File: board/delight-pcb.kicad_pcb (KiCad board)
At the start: 2 copper layers, 304.9 x 114.5 mm, 197 parts, among them J1 AVR-ISP-6, SW0 KEYSW, SW1 KEYSW, SW10 KEYSW, SW11 KEYSW, SW12 KEYSW, SW13 KEYSW, SW14 KEYSW, SW15 KEYSW, SW16 KEYSW, SW17 KEYSW, SW18 KEYSW, SW19 KEYSW, SW2 KEYSW, SW20 KEYSW, SW21 KEYSW, SW22 KEYSW, SW23 KEYSW, SW24 KEYSW, SW25 KEYSW, SW26 KEYSW, SW27 KEYSW, SW28 KEYSW, SW28-2 KEYSW, SW29 KEYSW, SW3 KEYSW, SW30 KEYSW, SW31 KEYSW, SW32 KEYSW, SW33 KEYSW, SW34 KEYSW, SW35 KEYSW, SW36 KEYSW, SW37 KEYSW, SW38 KEYSW, SW39 KEYSW, SW4 KEYSW, SW40 KEYSW, SW41 KEYSW, SW42 KEYSW, SW42-2 KEYSW, SW43 KEYSW, SW44 KEYSW, SW44-2 KEYSW, SW45 KEYSW, SW46 KEYSW, SW47 KEYSW, SW48 KEYSW, SW49 KEYSW, SW5 KEYSW, SW50 KEYSW, SW51 KEYSW, SW52 KEYSW, SW53 KEYSW, SW54 KEYSW, SW55 KEYSW, SW56 KEYSW, SW57 KEYSW, SW58 KEYSW, SW59 KEYSW, SW59-2 KEYSW, SW6 KEYSW, SW60 KEYSW, SW60-2 KEYSW, SW61 KEYSW, SW62-2 KEYSW, SW63 KEYSW, SW63-2 KEYSW, SW64 KEYSW, SW64-2 KEYSW, SW65 KEYSW, SW65-2 KEYSW, SW66 KEYSW, SW67 KEYSW, SW68 KEYSW, SW69 KEYSW, SW7 KEYSW, SW8 KEYSW, SW9 KEYSW, U1 ATmega32A-PU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

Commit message: Cleanup all the tracks after the footprint switch.
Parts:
- removed the REF** at (118.6, 115.6)
- removed the REF** at (71.9, 134.9)
- removed the REF** at (217.1, 178.4)
- added REF**: MountingHole_2.2mm_M2_Pad, MountingHole:MountingHole_2.2mm_M2_Pad, F.Cu at (205.7, 175.0)
- added REF**: MountingHole_2.2mm_M2_Pad, MountingHole:MountingHole_2.2mm_M2_Pad, F.Cu at (70.6, 135.4)
- moved REF** 40.4 mm to (348.7, 105.9)
- moved REF** 24.2 mm to (188.5, 133.9)
- moved REF** 23.1 mm to (350.3, 172.7)
- moved REF** 15.8 mm to (90.2, 173.5)
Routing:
- net Net-(D17-Pad2): track 138.9 -> 129.5 mm
- net row4: track 600.2 -> 607.7 mm
- net col1: track 163.5 -> 167.6 mm
- net Net-(D30-Pad2): track 152.6 -> 155.6 mm
- net Net-(D28-Pad2): track 56.2 -> 58.8 mm
- net Net-(D13-Pad2): track 67.2 -> 69.8 mm
- net Net-(D42-Pad2): track 81.2 -> 83.7 mm
- net Net-(D57-Pad2): track 72.5 -> 75.0 mm
- net Net-(D65-Pad2): track 21.1 -> 19.9 mm
- net Net-(D15-Pad2): track 155.7 -> 154.8 mm
- net col6: track 141.2 -> 142.1 mm
- net Net-(D3-Pad2): track 147.3 -> 146.7 mm
- net GND: vias 23 -> 22

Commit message: Traces for power and pairs
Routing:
- net col4: track 100.7 -> 106.7 mm
- net Net-(D1-Pad2): track 159.8 -> 164.5 mm
- net col10: track 210.2 -> 214.4 mm
- net Net-(D12-Pad2): track 79.4 -> 82.7 mm
- net col3: track 141.7 -> 145.0 mm
- net Net-(D27-Pad2): track 56.0 -> 59.3 mm
- net Net-(D47-Pad2): track 160.6 -> 157.7 mm
- net col11: track 213.2 -> 216.1 mm
- net Net-(D41-Pad2): track 70.0 -> 67.3 mm
- net Net-(D55-Pad2): track 91.9 -> 89.4 mm
- net Net-(D15-Pad2): track 154.8 -> 157.0 mm
- net col2: track 146.7 -> 148.9 mm
- net Net-(D11-Pad2): track 76.4 -> 78.4 mm
- net col12: track 226.8 -> 228.6 mm
- net Net-(D26-Pad2): track 55.0 -> 56.7 mm
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
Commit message: Footprint schema updated
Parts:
- D59, D60, D61, D62, D63, D64, D65, D66, D67, D68, D69: footprint cftkb:D_DO-35_SOD27_P5.08mm_Horizontal -> Diode_THT:D_DO-35_SOD27_P7.62mm_Horizontal
- moved D61 5.34 mm to (112.3, 174.0)
- moved D64 0.51 mm to (271.8, 174.0)
- moved D68 0.51 mm to (343.4, 174.0)
- moved D69 0.51 mm to (362.5, 174.0)
- moved D62 0.36 mm to (126.7, 174.0)
- moved D65 0.25 mm to (286.5, 174.0)
- moved D66 0.25 mm to (305.3, 174.0)
- moved D67 0.25 mm to (324.6, 174.0)
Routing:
- net Net-(D61-Pad2): track 16.9 -> 10.4 mm
- net row4: track 607.7 -> 602.3 mm
- net Net-(D64-Pad2): track 10.3 -> 11.3 mm
- net col14: track 267.3 -> 268.3 mm
- net col13: track 266.0 -> 267.0 mm
- net Net-(D62-Pad2): track 22.3 -> 23.1 mm
- net Net-(D66-Pad2): track 5.67 -> 6.19 mm
- net Net-(D63-Pad2): track 15.5 -> 15.0 mm
- net Net-(D60-Pad2): track 9.92 -> 9.39 mm
- net Net-(D69-Pad2): track 5.41 -> 5.93 mm
- net Net-(D68-Pad2): track 5.41 -> 5.93 mm

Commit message: Once more with layouts
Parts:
- moved D62 0.36 mm to (126.5, 173.7)
- moved D63 0.36 mm to (197.1, 173.7)
- moved D64 0.36 mm to (271.5, 173.7)
- moved D60 0.25 mm to (85.6, 173.7)
- moved D61 0.25 mm to (112.3, 173.7)
- moved D65 0.25 mm to (286.5, 173.7)
- moved D66 0.25 mm to (305.3, 173.7)
- moved D67 0.25 mm to (324.6, 173.7)
- moved D68 0.25 mm to (343.4, 173.7)
- moved D69 0.25 mm to (362.5, 173.7)
- moved D59 0.25 mm to (85.6, 154.7)
- moved SW63 0.17 mm to (195.9, 182.4)
- moved SW61 0.15 mm to (100.3, 182.4)
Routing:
- net row4: track 602.3 -> 601.2 mm
- net Net-(D69-Pad2): track 5.93 -> 6.69 mm
- net Net-(D68-Pad2): track 5.93 -> 6.69 mm
- net Net-(D67-Pad2): track 6.08 -> 6.59 mm
- net Net-(D66-Pad2): track 6.19 -> 6.70 mm
- net Net-(D65-Pad2): track 20.3 -> 20.8 mm

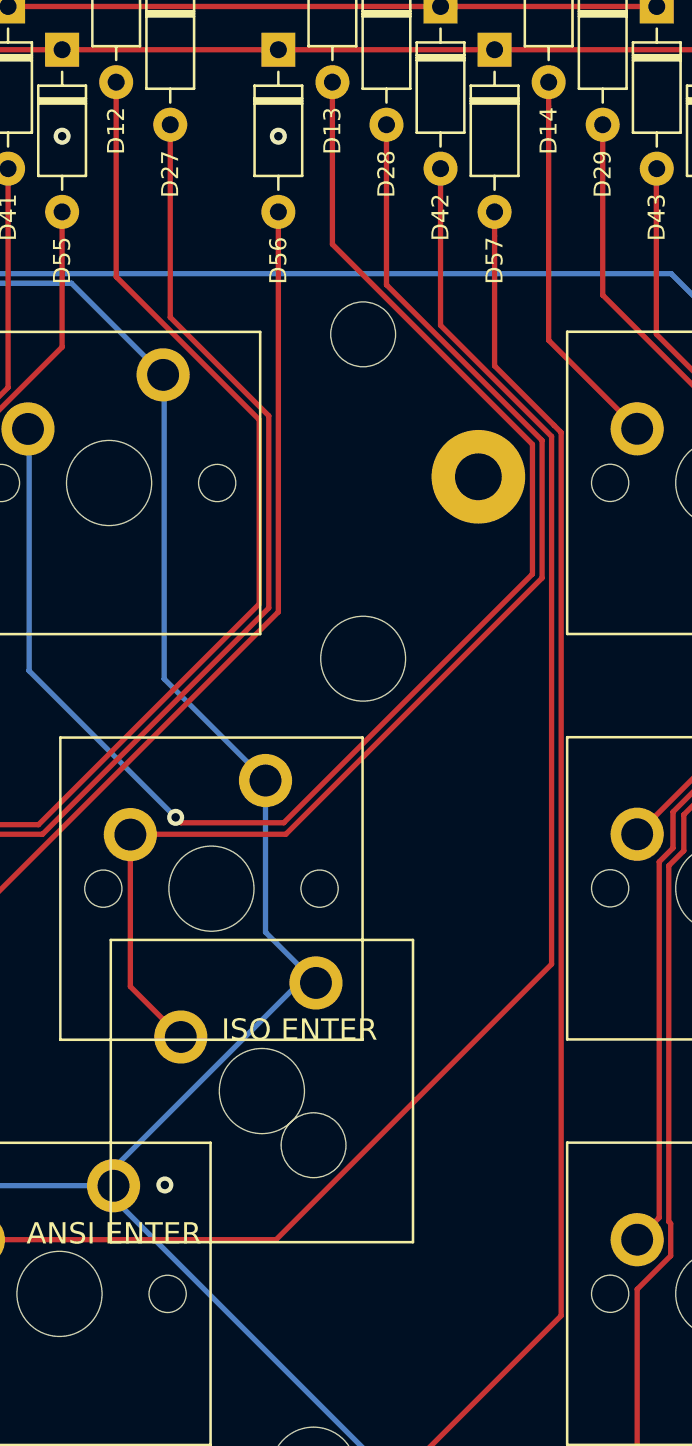
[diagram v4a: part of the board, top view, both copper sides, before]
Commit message: mounting holes movement.
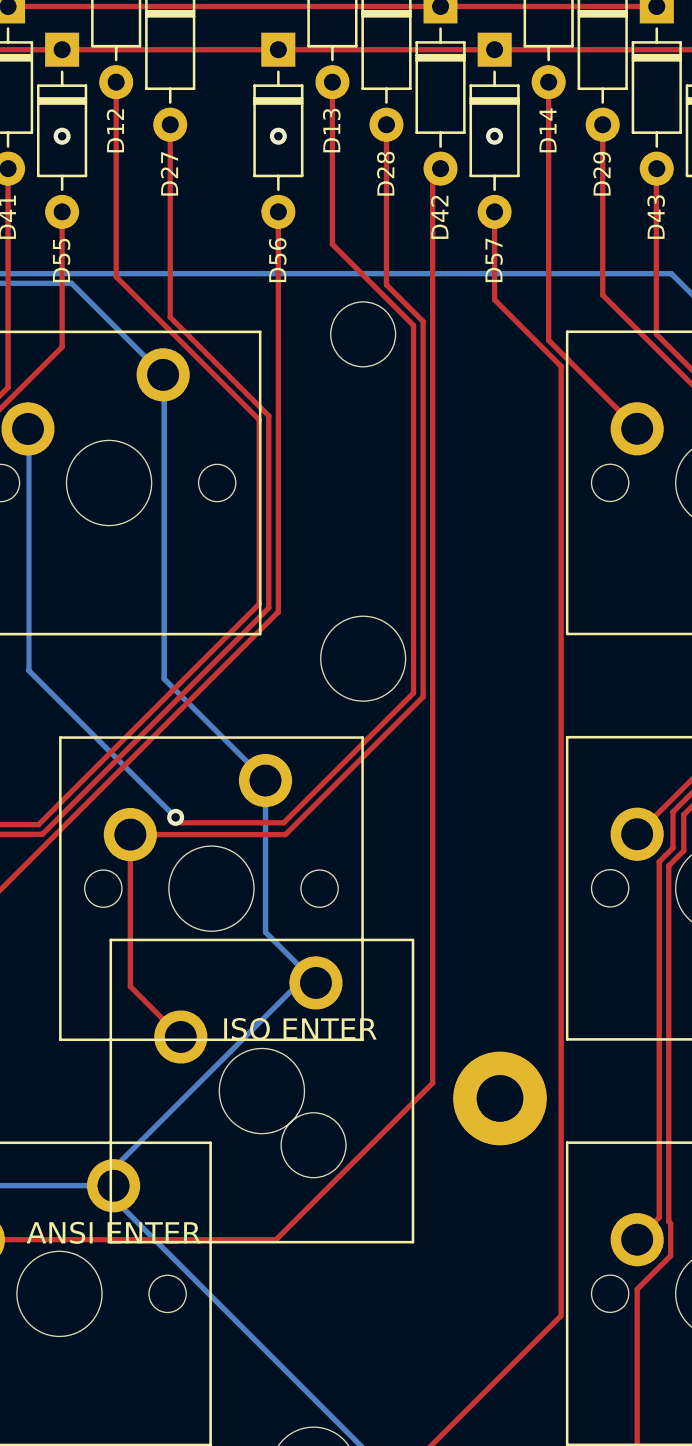
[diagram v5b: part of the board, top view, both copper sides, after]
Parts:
- moved REF** 29.2 mm to (349.8, 135.1)
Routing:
- net Net-(D13-Pad2): track 69.8 -> 65.2 mm
- net Net-(D28-Pad2): track 59.2 -> 54.5 mm
- net Net-(D42-Pad2): track 83.7 -> 79.4 mm
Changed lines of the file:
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@@
     (thickness 1.6)
     (drawings 36)
-    (tracks 1179)
+    (tracks 1175)
     (zones 0)
     (modules 196)
@@
   )
   (module MountingHole:MountingHole_2.2mm_M2_Pad (layer F.Cu)
-    (at 348.742 105.918)
+    (at 349.758 135.128)
     (descr "Mounting Hole 2.2mm, M2")
     (tags "mounting hole 2.2mm m2")
@@
   (via (at 339.344 89.916) (size 0.8) (drill 0.4) (layers F.Cu B.Cu) (net 1))
   (via (at 298.196 120.142) (size 0.8) (drill 0.4) (layers F.Cu B.Cu) (net 1))
-  (via (at 334.01 139.192) (size 0.8) (drill 0.4) (layers F.Cu B.Cu) (net 1))
-  (via (at 317.5 120.142) (size 0.8) (drill 0.4) (layers F.Cu B.Cu) (net 1))
   (via (at 290.322 178.562) (size 0.8) (drill 0.4) (layers F.Cu B.Cu) (net 1))
   (via (at 322.58 140.462) (size 0.8) (drill 0.4) (layers F.Cu B.Cu) (net 1))
+  (via (at 349.504 89.916) (size 0.8) (drill 0.4) (layers F.Cu B.Cu) (net 1))
+  (via (at 317.5 120.142) (size 0.8) (drill 0.4) (layers F.Cu B.Cu) (net 1))
   (segment (start 122.008 81.495) (end 122.008 82.245) (width 0.381) (layer F.Cu) (net 2))
   (segment (start 117.758 82.245) (end 117.758 81.495) (width 0.381) (layer F.Cu) (net 2))
@@
   (segment (start 310.388 121.92) (end 310.73174 122.26374) (width 0.25) (layer F.Cu) (net 15))
   (segment (start 327.62825 103.66375) (end 327.62825 115.03025) (width 0.25) (layer B.Cu) (net 16))
-  (segment (start 334.518 121.92) (end 334.772 122.174) (width 0.25) (layer F.Cu) (net 16) (status 40000))
-  (segment (start 334.772 122.174) (end 339.598 122.174) (width 0.25) (layer F.Cu) (net 16) (status 40000))
-  (segment (start 339.598 122.174) (end 351.282 110.49) (width 0.25) (layer F.Cu) (net 16) (status 40000))
-  (segment (start 351.282 110.49) (end 351.282 104.394) (width 0.25) (layer F.Cu) (net 16) (status 40000))
-  (segment (start 351.282 104.394) (end 341.884 94.996) (width 0.25) (layer F.Cu) (net 16) (status 40000))
-  (segment (start 341.884 94.996) (end 341.884 87.376) (width 0.25) (layer F.Cu) (net 16) (status 40000))
   (via (at 334.518 121.92) (size 0.8) (drill 0.4) (layers F.Cu B.Cu) (net 16))
   (segment (start 327.62825 115.03025) (end 334.518 121.92) (width 0.25) (layer B.Cu) (net 16))
+  (segment (start 345.694 98.806) (end 341.884 94.996) (width 0.25) (layer F.Cu) (net 16))
+  (segment (start 345.694 116.078) (end 345.694 98.806) (width 0.25) (layer F.Cu) (net 16) (status 40000))
+  (segment (start 341.884 94.996) (end 341.884 87.376) (width 0.25) (layer F.Cu) (net 16))
+  (segment (start 339.598 122.174) (end 345.694 116.078) (width 0.25) (layer F.Cu) (net 16))
+  (segment (start 334.772 122.174) (end 339.598 122.174) (width 0.25) (layer F.Cu) (net 16))
+  (segment (start 334.518 121.92) (end 334.772 122.174) (width 0.25) (layer F.Cu) (net 16))
   (segment (start 352.044 88.50737) (end 352.044 87.376) (width 0.25) (layer F.Cu) (net 17))
-  (segment (start 352.044 99.5045) (end 352.044 88.50737) (width 0.25) (layer F.Cu) (net 17))
-  (segment (start 356.20325 103.66375) (end 352.044 99.5045) (width 0.25) (layer F.Cu) (net 17))
+  (segment (start 352.044 99.5045) (end 352.044 88.50737) (width 0.25) (layer F.Cu) (net 17) (status 40000))
+  (segment (start 356.20325 103.66375) (end 352.044 99.5045) (width 0.25) (layer F.Cu) (net 17) (status 40000))
   (segment (start 212.344 97.27918) (end 212.344 89.376) (width 0.25) (layer F.Cu) (net 18) (status 40000))
   (segment (start 211.405208 98.217972) (end 212.344 97.27918) (width 0.25) (layer F.Cu) (net 18) (status 40000))
@@
   (segment (start 338.89399 112.0816) (end 338.893989 103.053579) (width 0.25) (layer F.Cu) (net 31))
   (segment (start 338.893989 103.053579) (end 334.264 98.42359) (width 0.25) (layer F.Cu) (net 31))
-  (segment (start 344.424 96.89959) (end 344.424 89.376) (width 0.25) (layer F.Cu) (net 32))
-  (segment (start 351.732009 104.207599) (end 344.424 96.89959) (width 0.25) (layer F.Cu) (net 32))
-  (segment (start 339.69466 122.71375) (end 351.73201 110.6764) (width 0.25) (layer F.Cu) (net 32))
-  (segment (start 332.39 122.73) (end 332.40625 122.71375) (width 0.25) (layer F.Cu) (net 32))
-  (segment (start 332.40625 122.71375) (end 339.69466 122.71375) (width 0.25) (layer F.Cu) (net 32))
   (segment (start 332.39 129.87) (end 332.39 122.73) (width 0.25) (layer F.Cu) (net 32))
   (segment (start 334.75875 132.23875) (end 332.39 129.87) (width 0.25) (layer F.Cu) (net 32))
-  (segment (start 351.73201 110.6764) (end 351.732009 104.207599) (width 0.25) (layer F.Cu) (net 32))
   (segment (start 334.772 132.23875) (end 334.75875 132.23875) (width 0.25) (layer F.Cu) (net 32))
+  (segment (start 346.14401 98.6196) (end 344.424 96.89959) (width 0.25) (layer F.Cu) (net 32))
+  (segment (start 339.67841 122.73) (end 346.14401 116.2644) (width 0.25) (layer F.Cu) (net 32))
+  (segment (start 332.39 122.73) (end 339.67841 122.73) (width 0.25) (layer F.Cu) (net 32))
+  (segment (start 346.14401 116.2644) (end 346.14401 98.6196) (width 0.25) (layer F.Cu) (net 32))
+  (segment (start 344.424 96.89959) (end 344.424 89.376) (width 0.25) (layer F.Cu) (net 32))
   (segment (start 354.584 97.381996) (end 354.584 89.376) (width 0.25) (layer F.Cu) (net 33))
   (segment (start 356.20325 122.71375) (end 362.458 116.459) (width 0.25) (layer F.Cu) (net 33))
@@
   (segment (start 325.24725 141.76375) (end 313.34075 141.76375) (width 0.25) (layer B.Cu) (net 47))
   (segment (start 339.235252 141.76375) (end 325.24725 141.76375) (width 0.25) (layer F.Cu) (net 47))
-  (segment (start 352.182019 128.816983) (end 339.235252 141.76375) (width 0.25) (layer F.Cu) (net 47))
-  (segment (start 352.182019 104.0212) (end 352.182019 128.816983) (width 0.25) (layer F.Cu) (net 47) (status 40000))
-  (segment (start 346.964 98.80318) (end 352.182019 104.0212) (width 0.25) (layer F.Cu) (net 47))
-  (segment (start 346.964 91.44) (end 346.964 98.80318) (width 0.25) (layer F.Cu) (net 47))
+  (segment (start 346.594021 91.809979) (end 346.594021 134.404981) (width 0.25) (layer F.Cu) (net 47))
+  (segment (start 346.594021 134.404981) (end 339.235252 141.76375) (width 0.25) (layer F.Cu) (net 47))
+  (segment (start 346.964 91.44) (end 346.594021 91.809979) (width 0.25) (layer F.Cu) (net 47))
   (segment (start 357.103271 99.216358) (end 357.103271 91.460729) (width 0.25) (layer F.Cu) (net 48))
   (segment (start 362.908009 105.021096) (end 357.103271 99.216358) (width 0.25) (layer F.Cu) (net 48))
@@
   (segment (start 310.642 160.4965) (end 310.642 140.97) (width 0.25) (layer F.Cu) (net 62))
   (segment (start 310.95925 160.81375) (end 310.642 160.4965) (width 0.25) (layer F.Cu) (net 62))
-  (segment (start 349.504 94.60337) (end 349.504 93.472) (width 0.25) (layer F.Cu) (net 63))
-  (segment (start 349.504 100.706769) (end 349.504 94.60337) (width 0.25) (layer F.Cu) (net 63))
-  (segment (start 352.298 103.500769) (end 349.504 100.706769) (width 0.25) (layer F.Cu) (net 63))
-  (segment (start 352.632029 145.334971) (end 352.632028 103.834799) (width 0.25) (layer F.Cu) (net 63))
-  (segment (start 352.632028 103.834799) (end 352.298 103.500769) (width 0.25) (layer F.Cu) (net 63))
+  (segment (start 349.504 97.60091) (end 349.504 93.472) (width 0.25) (layer F.Cu) (net 63))
+  (segment (start 352.632029 100.728939) (end 349.504 97.60091) (width 0.25) (layer F.Cu) (net 63))
+  (segment (start 352.632029 145.334971) (end 352.632029 100.728939) (width 0.25) (layer F.Cu) (net 63))
   (segment (start 337.15325 160.81375) (end 352.632029 145.334971) (width 0.25) (layer F.Cu) (net 63))
   (segment (start 356.20325 159.045984) (end 356.20325 160.81375) (width 0.25) (layer F.Cu) (net 64))

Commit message: More project cleanup
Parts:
- removed the G*** at (166.5, 182.3) (x2)
- removed the G*** at (166.3, 182.3) (x2)
- removed the G*** at (166.1, 178.1) (x2)
- added G***: LOGO, Lotier:lotier_rev1, B.Cu at (164.3, 186.2)
- added G***: LOGO, Lotier:lotier_rev1, F.Cu at (164.1, 182.4)
- added G***: LOGO, Lotier:lotier_rev1_16mm_mask, F.Cu at (166.4, 182.4)
- F1: footprint project:Bourns-MF-R050-0-0-MFG -> Fuse:Fuse_Bourns_MF-RHT050
- G*** (x2): footprint cftkb:DELIGHT_SMALL_COPPER -> Lotier:DELIGHT_SMALL
- moved REF** 19.6 mm to (90.2, 134.1)
- moved REF** 19.3 mm to (207.8, 134.1)
- moved F1 2.58 mm to (112.8, 94.2)
- moved REF** 2.54 mm to (207.8, 173.5)
- moved G*** 2.29 mm to (163.8, 178.1) (x2)
- moved REF** 1.27 mm to (350.5, 134.1)
- moved REF** 0.80 mm to (350.5, 173.5)
- moved RESET1 0.36 mm to (93.5, 80.0)
- moved BOOT1 0.25 mm to (105.4, 80.0)
- moved ST63 0.15 mm to (195.9, 182.4)
- moved SW65 0.14 mm to (283.8, 182.4)
- moved SW65-2 0.07 mm to (298.1, 182.4)
- moved SW64 0.06 mm to (264.8, 182.4)
- moved SW44 0.05 mm to (81.4, 144.3)
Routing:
- net Net-(D57-Pad2): track 75.0 -> 72.5 mm
- net GND: track 8.36 -> 6.80 mm
- net Net-(D71-Pad1): track 28.7 -> 30.1 mm
- net row4: track 601.2 -> 602.1 mm
- net Net-(R1-Pad2): track 13.5 -> 14.3 mm
- net Net-(R2-Pad1): vias 1 -> 0

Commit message: Hotswap created and routed
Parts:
- removed the G*** at (164.3, 186.2)
- removed the G*** at (164.1, 182.4)
- removed ST63-2: 7U, stabs:Stabilizer_Cherry_MX_7u
- removed SW28-2: KEYSW, cherrymx:SW_Cherry_MX_Plate_ISOEnter
- removed SW42-2, SW45, SW63-2: KEYSW, cherrymx:SW_Cherry_MX_PCB_1.00u
- removed SW44-2, SW59-2: KEYSW, cherrymx:SW_Cherry_MX_PCB_1.25u
- removed SW60-2, SW62-2, SW64-2, SW65-2: KEYSW, cherrymx:SW_Cherry_MX_PCB_1.50u
- G*** (x2): footprint Lotier:DELIGHT_SMALL -> Lotier:DETACH_SMALL
- SW0, SW1, SW10, SW11, SW12, SW14, SW15, SW16, SW17, SW18, SW19, SW2, SW20, SW21, SW22, SW23, SW24, SW25, SW26, SW27, SW29, SW3, SW31, SW32, SW33, SW34, SW35, SW36, SW37, SW38, SW39, SW4, SW40, SW41, SW43, SW46, SW47, SW48, SW49, SW5, SW50, SW51, SW52, SW53, SW54, SW55, SW57, SW58, SW6, SW66, SW67, SW68, SW69, SW7, SW8, SW9: footprint cherrymx:SW_Cherry_MX_PCB_1.00u -> Switch_Keyboard_Kailh:SW_Hotswap_Kailh_1.00u
- SW13: footprint cherrymx:SW_Cherry_MX_PCB_2.00u -> Switch_Keyboard_Kailh:SW_Hotswap_Kailh_2.00u
- SW28, SW30: footprint cherrymx:SW_Cherry_MX_PCB_1.50u -> Switch_Keyboard_Kailh:SW_Hotswap_Kailh_1.50u
- SW42, SW59: footprint cherrymx:SW_Cherry_MX_PCB_2.25u -> Switch_Keyboard_Kailh:SW_Hotswap_Kailh_2.25u
- SW44, SW56: footprint cherrymx:SW_Cherry_MX_PCB_1.75u -> Switch_Keyboard_Kailh:SW_Hotswap_Kailh_1.75u
- SW60, SW61: footprint cherrymx:SW_Cherry_MX_PCB_1.25u -> Switch_Keyboard_Kailh:SW_Hotswap_Kailh_1.25u
- SW62: renamed from S62; footprint cherrymx:SW_Cherry_MX_PCB_1.25u -> Switch_Keyboard_Kailh:SW_Hotswap_Kailh_1.25u
- SW63: footprint cherrymx:SW_Cherry_MX_PCB_1.00u -> Switch_Keyboard_Kailh:SW_Hotswap_Kailh_6.25u
- SW64, SW65: footprint cherrymx:SW_Cherry_MX_PCB_1.25u -> Switch_Keyboard_Kailh:SW_Hotswap_Kailh_1.00u
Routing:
- net Net-(D45-Pad2): track 175.4 -> 121.9 mm
- net col0: track 195.2 -> 163.9 mm
- net col3: track 145.0 -> 122.4 mm
- net Net-(D62-Pad2): track 23.1 -> 6.83 mm
- net Net-(D65-Pad2): track 20.8 -> 7.17 mm
- net Net-(D57-Pad2): track 72.5 -> 84.3 mm, vias 0 -> 1
- net col13: track 267.0 -> 255.7 mm
- net Net-(D56-Pad2): track 79.4 -> 90.6 mm, vias 0 -> 1
- net col10: track 214.4 -> 203.4 mm
- net col1: track 168.7 -> 157.8 mm
- net Net-(D59-Pad2): track 16.8 -> 7.23 mm
- net Net-(D51-Pad2): track 131.6 -> 140.6 mm, vias 0 -> 1
- net Net-(D63-Pad2): track 15.4 -> 6.47 mm
- net Net-(D53-Pad2): track 104.4 -> 113.3 mm, vias 0 -> 1
- net Net-(D47-Pad2): track 157.7 -> 166.6 mm, vias 0 -> 1
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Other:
- board text removed: "1.25U ISO"
- board text removed: "1.5U"
- board text removed: "1U ISO"
- board text removed: "ISO ENTER"
- board text removed: "STEPPED"
